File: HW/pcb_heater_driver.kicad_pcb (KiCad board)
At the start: 2 copper layers, 160 x 100 mm, 64 parts, among them J1 Heater, J2 JTAG, J4 USB_C_Receptacle_USB2.0, J5 OLED, Q1 RQ3E110AJ, Q2 BC817, Q3 BC817, SW1 SW_SPST, SW2 SW_DPST, SW3 SW_DPST, SW4 SW_SPST, SW5 SW_SPST, U1 ESP32-S2-MINI-2, U2 TS30042-M000QFNR, U3 CH340C, U4 fork_p5.0mm, U5 fork_p5.0mm

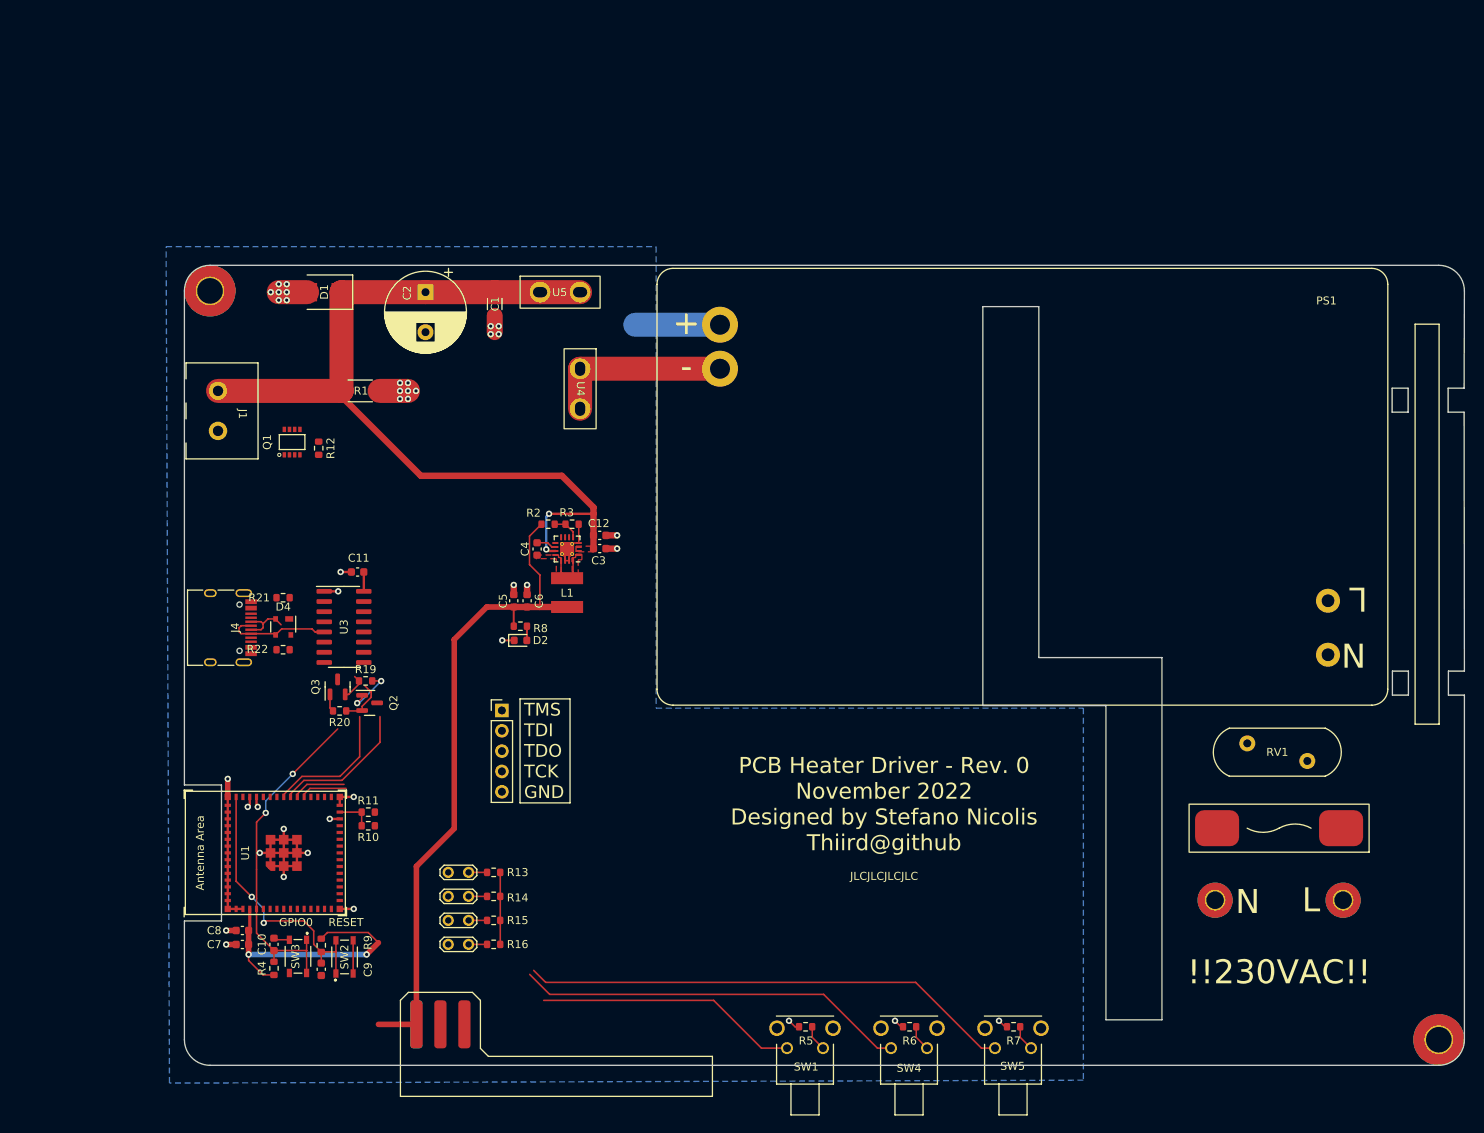
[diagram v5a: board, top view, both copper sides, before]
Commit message: Finished routing, only mosfet left, fixed layout, outline
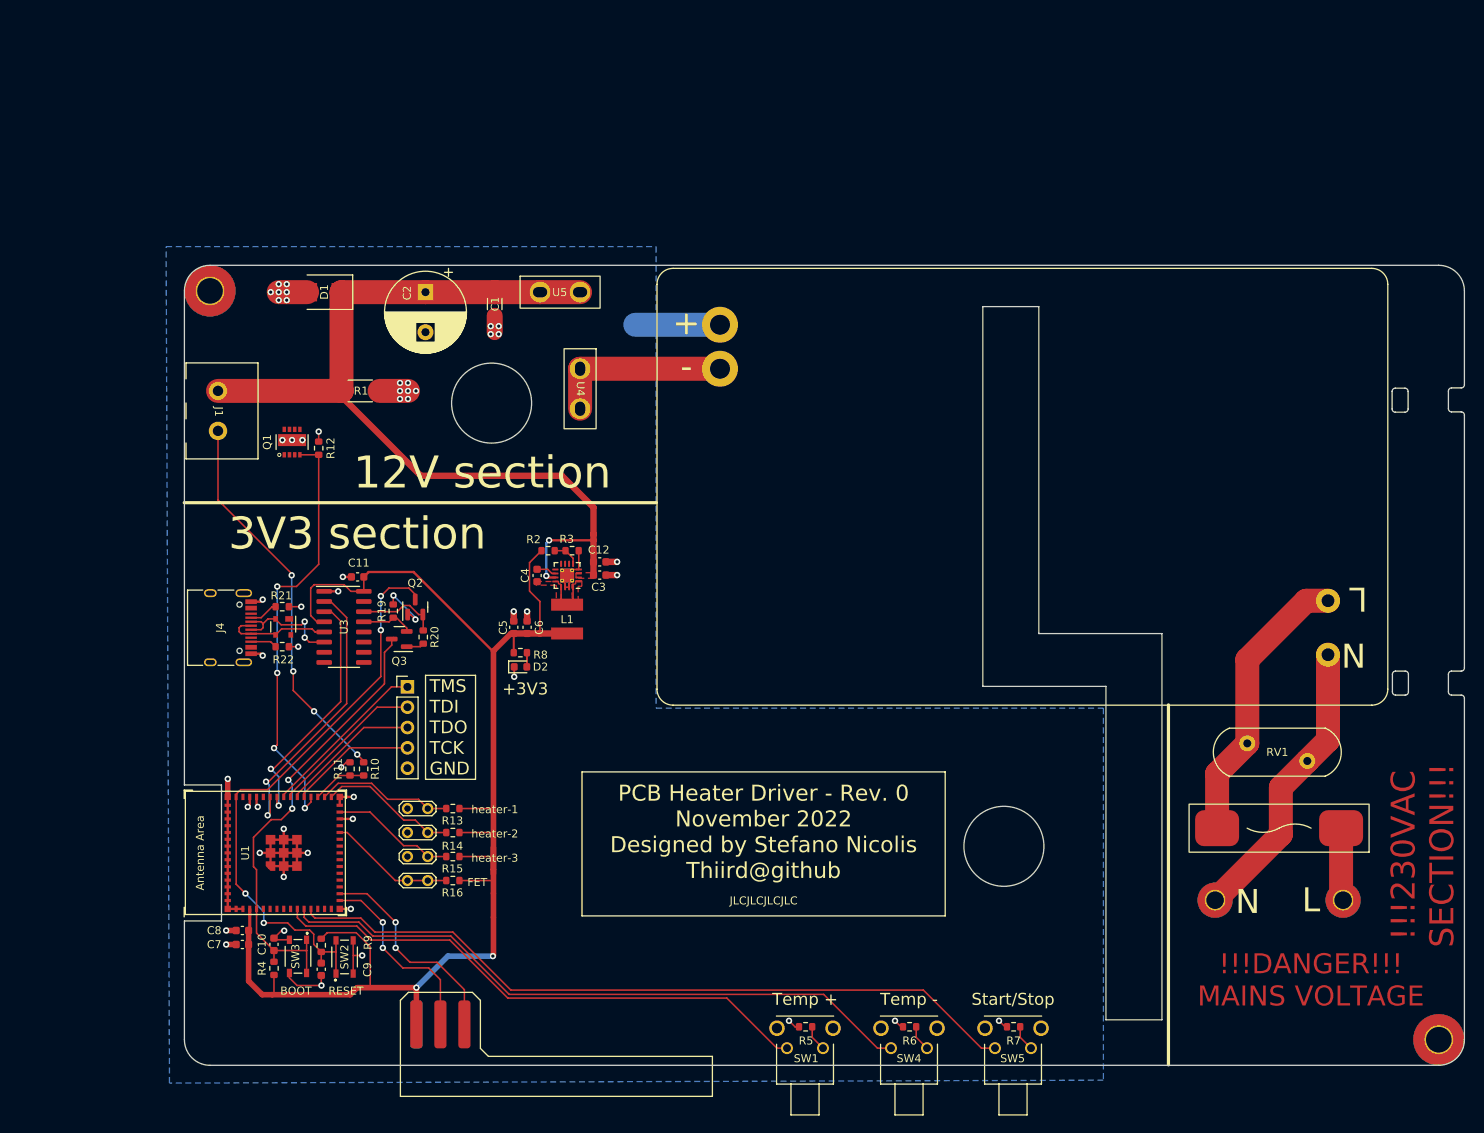
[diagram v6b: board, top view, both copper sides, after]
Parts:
- moved R20 13.9 mm to (103.0, 91.6), turned to -90 degrees
- moved Q2 13.3 mm to (102.0, 87.9), turned to 90 degrees
- moved J2 12.2 mm to (101.0, 97.8)
- moved Q3 9.75 mm to (100.0, 91.9), turned to 180 degrees
- moved R15 9.47 mm to (106.7, 119.0)
- moved R16 9.47 mm to (106.7, 122.0)
- moved TH1 9.47 mm to (101.0, 113.0)
- moved TH3 9.47 mm to (101.0, 119.0)
- moved TH4 9.47 mm to (101.0, 122.0)
- moved R13 9.47 mm to (106.7, 113.0)
- moved R14 9.47 mm to (106.7, 116.0)
- moved TH2 9.47 mm to (101.0, 116.0)
- moved R19 9.39 mm to (99.2, 88.4), turned to 90 degrees
- moved R10 7.13 mm to (95.5, 108.1), turned to -90 degrees
- moved R11 5.86 mm to (93.8, 108.1), turned to 90 degrees
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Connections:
- SW5 pad 1: user_action -> start_stop
- U1 pad 10: user_action -> temperature_plus
- U1 pad 11: temperature_plus -> temperature_minus
- U1 pad 12: temperature_minus -> start_stop
- U1 pad 29: current_sense_LOW -> temp_heater_3
- U1 pad 31: temp_heater_3 -> temp_heater_2
- U1 pad 32: temp_heater_2 -> temp_heater_1
- U1 pad 33: temp_heater_1 -> current_sense_LOW
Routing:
- net start_stop: track 0.00 -> 93.1 mm
- net user_action: track 61.7 -> 0.00 mm
- net GPIO0: track 0.29 -> 58.2 mm, vias 0 -> 2
- net mosfet_gate: track 0.00 -> 53.5 mm, vias 0 -> 4
- net /Heater/heater_LOW: track 0.00 -> 49.0 mm, vias 0 -> 7
- net +3V3: track 131.3 -> 179.4 mm
- net RESET: track 34.7 -> 74.5 mm, vias 2 -> 4
- net Net-(H7-Pad1): track 0.00 -> 36.5 mm
- net temperature_plus: track 32.9 -> 69.1 mm
- net Net-(F1-Pad2): track 0.00 -> 35.8 mm
- net RX: track 0.00 -> 35.4 mm, vias 0 -> 2
- net temperature_minus: track 49.0 -> 81.2 mm
- net TX: track 0.00 -> 31.0 mm, vias 0 -> 2
- net SDA: track 0.00 -> 26.8 mm, vias 0 -> 2
- net GND: track 142.4 -> 116.9 mm, vias 42 -> 49
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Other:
- outline, holes or cut-outs redrawn
- board text added: "!!!230VAC SECTION!!!"
- board text added: "!!!DANGER!!! MAINS VOLTAGE"
- board text added: "+3V3"
- board text added: "12V section"
- board text added: "3V3 section"
- board text added: "BOOT"
- board text added: "FET"
- board text added: "Start/Stop"
- board text added: "Temp +"
- board text added: "Temp -"
- board text added: "heater-1"
- board text added: "heater-2"
- board text added: "heater-3"
- board text removed: "!!230VAC!!"
- board text removed: "GPIO0"

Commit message: Fix board, QOL fixes
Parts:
- moved R10 6.69 mm to (88.9, 109.2), turned to 180 degrees
- moved SW2 5.65 mm to (87.5, 131.5), turned to -90 degrees
- moved R11 4.94 mm to (88.9, 107.5), turned to 0 degrees
- moved SW3 4.73 mm to (82.6, 131.5)
- moved U1 4.73 mm to (80.8, 118.6)
- moved C10 4.73 mm to (79.6, 130.0)
- moved C7 4.73 mm to (75.6, 130.0)
- moved C8 4.73 mm to (75.6, 128.3)
- moved R4 4.73 mm to (79.6, 133.0)
- moved C9 3.17 mm to (90.4, 130.0), turned to 90 degrees
- moved R9 2.84 mm to (90.4, 133.0), turned to 90 degrees
- moved Q1 0.83 mm to (87.1, 66.6)
- moved R12 0.83 mm to (90.5, 67.4)
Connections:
- U1 pad 28: GND -> unconnected-(U1-Pad28)
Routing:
- net +3V3: track 179.4 -> 172.3 mm
- net RESET: track 74.5 -> 81.0 mm
- net /MCU/TMS: track 21.3 -> 26.4 mm
- net /MCU/TCK: track 15.7 -> 20.6 mm
- net /MCU/TDO: track 17.6 -> 22.4 mm
- net /MCU/TDI: track 19.5 -> 24.3 mm
- net temp_heater_3: track 15.6 -> 20.3 mm
- net start_stop: track 93.1 -> 97.8 mm
- net temp_mosfet: track 15.8 -> 20.5 mm
- net temperature_plus: track 69.1 -> 73.7 mm
- net temp_heater_1: track 17.2 -> 21.9 mm
- net temperature_minus: track 81.2 -> 85.7 mm
- net SCL: track 24.1 -> 28.6 mm
- net temp_heater_2: track 17.3 -> 21.8 mm
- net GPIO0: track 58.2 -> 62.4 mm
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- added copper zone on B.Cu, net /Heater/heater_LOW
- added copper zone on F.Cu, net /Heater/heater_LOW
- added copper zone on F.Cu, net GND
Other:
- outline, holes or cut-outs redrawn

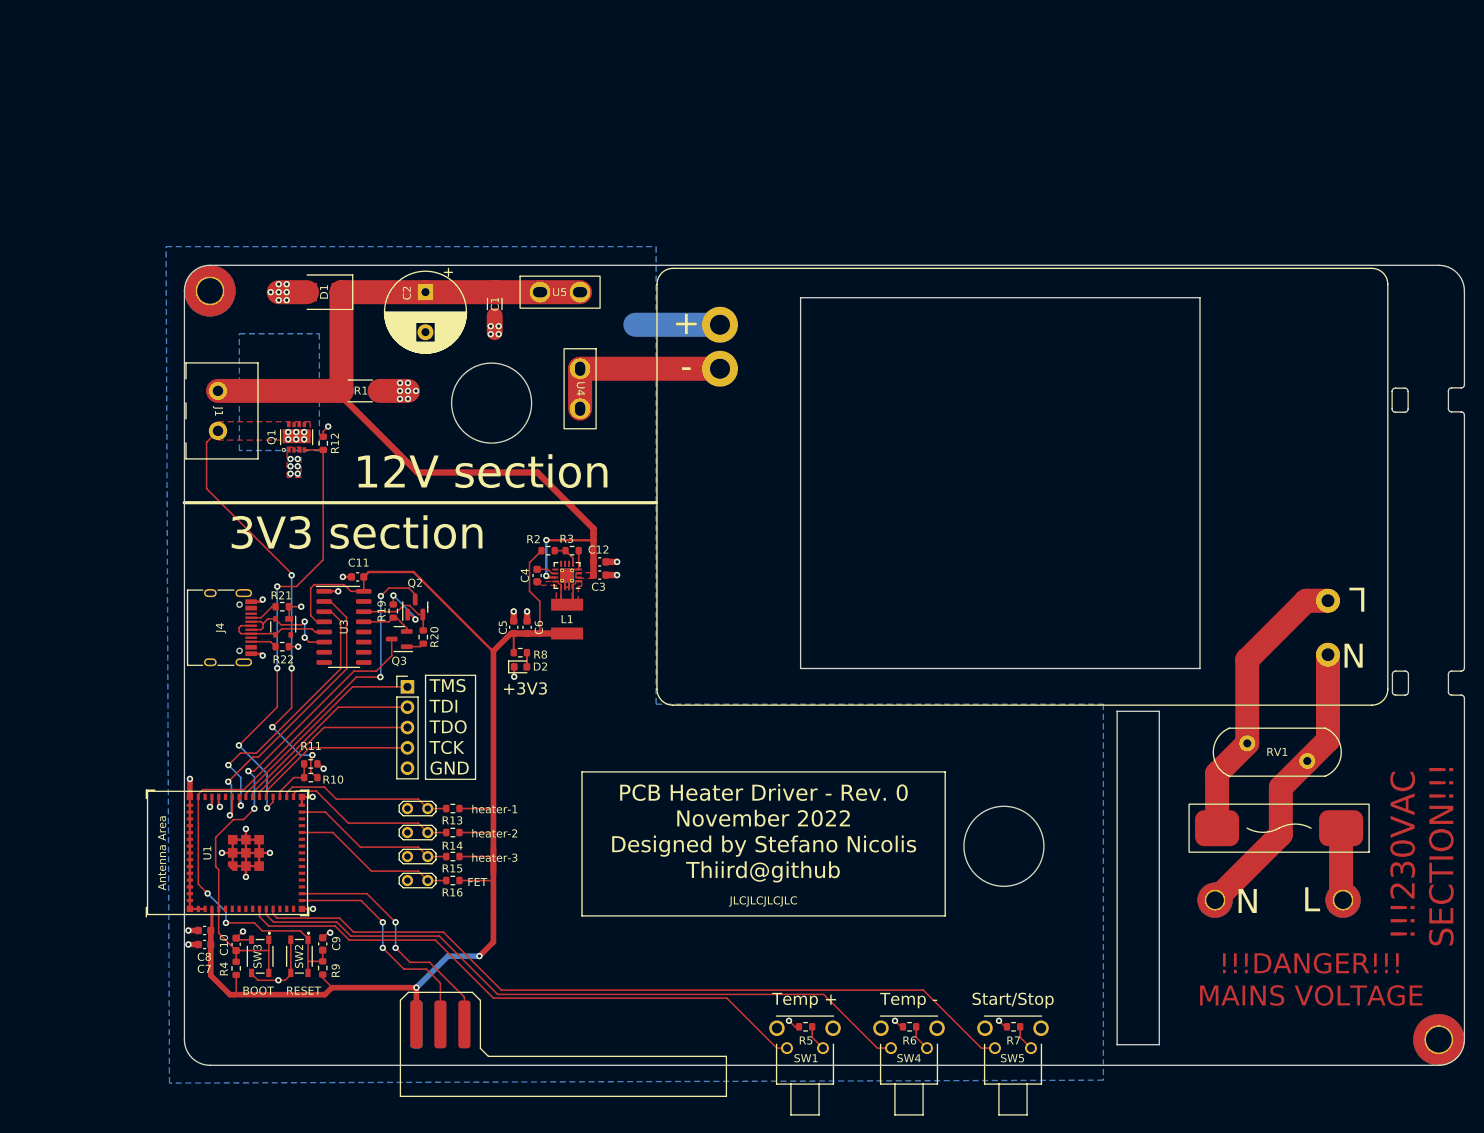
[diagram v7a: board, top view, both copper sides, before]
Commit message: QOL changes on pcb, fixed wrong ACDC brick polarity xD
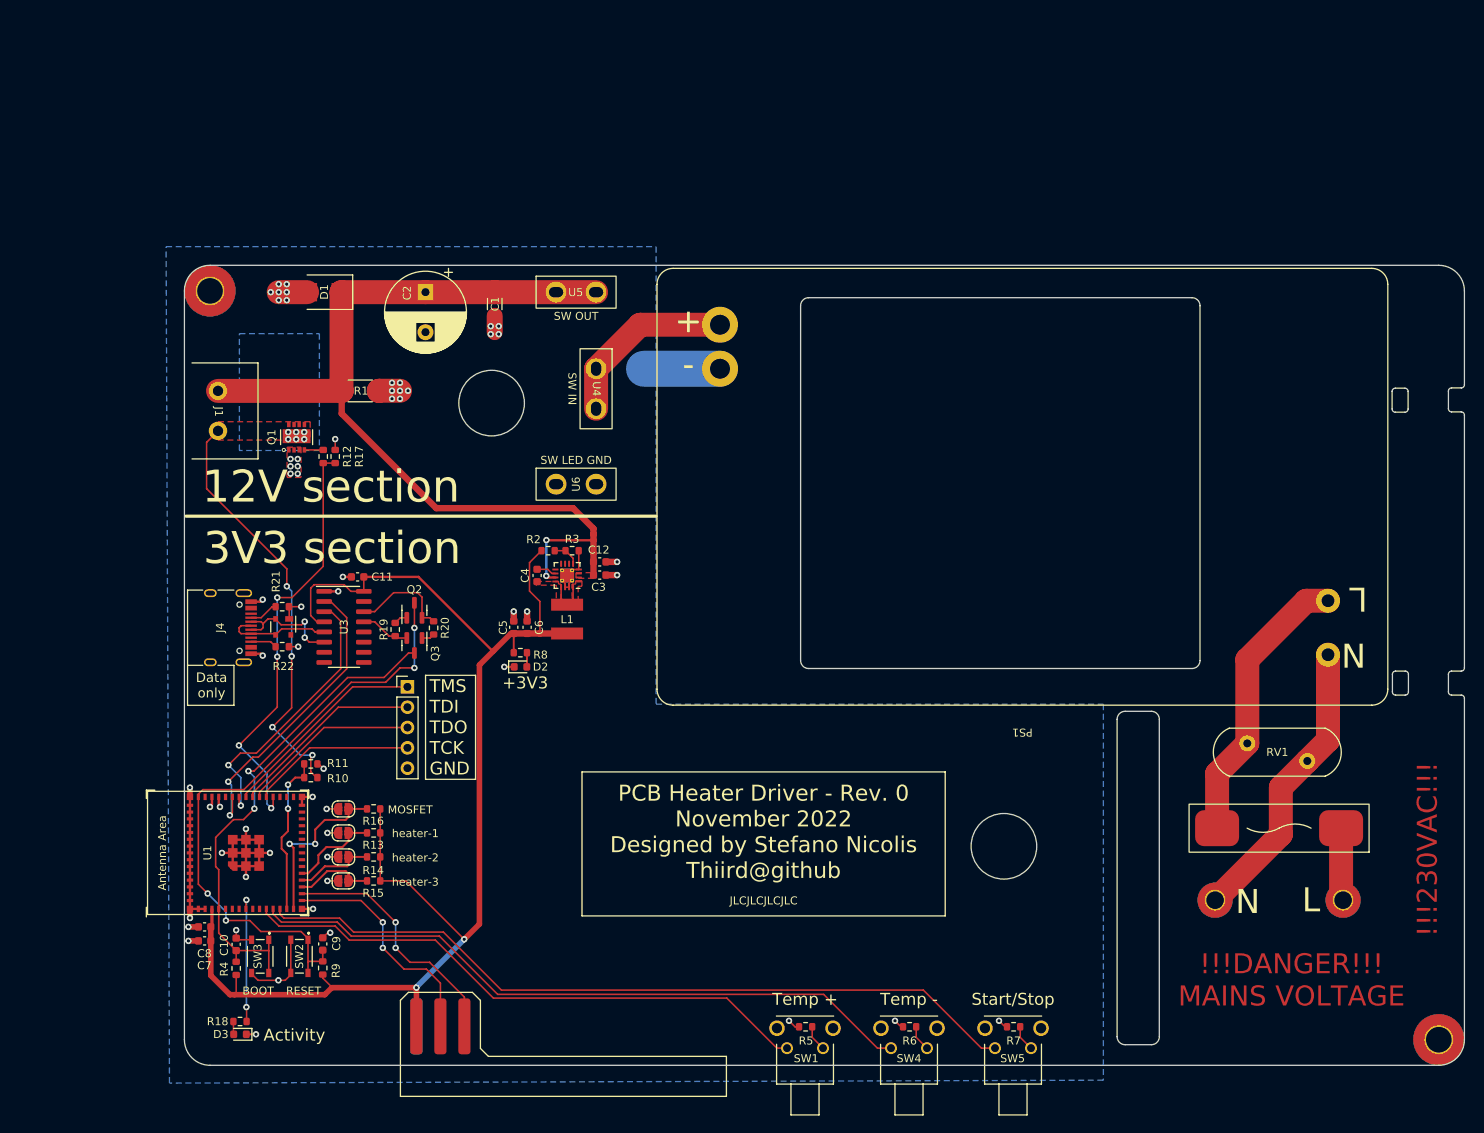
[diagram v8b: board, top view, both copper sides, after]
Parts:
- added D3: RED, LED_SMD:LED_0603_1608Metric, F.Cu at (80.1, 141.3)
- added R17: TBD, Resistor_SMD:R_0603_1608Metric, F.Cu at (90.5, 69.0)
- added R18: 1k, Resistor_SMD:R_0603_1608Metric, F.Cu at (80.1, 139.7)
- added U6: fork_p5.0mm, fork_connector_p5.0mm:fork_p5.0mm, F.Cu at (122.1, 72.5)
- R10: value 100k -> 22k
- R11: value 37k -> 5k1
- TH1, TH2, TH3, TH4: footprint TestPoint:TestPoint_2Pads_Pitch2.54mm_Drill0.8mm -> Jumper:SolderJumper-2_P1.3mm_Open_RoundedPad1.0x1.5mm
- moved R16 13.4 mm to (96.8, 113.1)
- moved TH4 12.0 mm to (93.0, 113.1)
- moved R15 10.4 mm to (96.8, 122.1)
- moved R13 10.4 mm to (96.8, 116.1)
- moved R14 10.4 mm to (96.8, 119.1)
- moved TH1 8.56 mm to (93.0, 116.1)
- moved TH3 8.56 mm to (93.0, 122.1)
- moved TH2 8.56 mm to (93.0, 119.1)
- moved R19 2.32 mm to (99.5, 90.7)
- moved R12 2.23 mm to (92.0, 69.0)
- moved Q3 2.06 mm to (101.9, 92.7), turned to -90 degrees
- moved U4 2.00 mm to (124.6, 60.6)
- moved U5 2.00 mm to (122.1, 48.5)
- moved R20 1.73 mm to (104.3, 90.5)
- moved C7 0.45 mm to (75.6, 129.6)
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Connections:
- PS1 pad 3: GND -> Net-(PS1-Pad3)
- PS1 pad 4: Net-(PS1-Pad4) -> GND
- Q1 pad 2: mosfet_gate -> Net-(Q1-Pad2)
- U1 pad 10: temperature_plus -> unconnected-(U1-Pad10)
- U1 pad 11: temperature_minus -> temperature_plus
- U1 pad 12: start_stop -> temperature_minus
- U1 pad 13: unconnected-(U1-Pad13) -> start_stop
- U1 pad 14: unconnected-(U1-Pad14) -> current_sense_LOW
- U1 pad 15: unconnected-(U1-Pad15) -> temp_mosfet
- U1 pad 18: unconnected-(U1-Pad18) -> temp_heater_3
- U1 pad 19: unconnected-(U1-Pad19) -> temp_heater_2
- U1 pad 20: unconnected-(U1-Pad20) -> temp_heater_1
- U1 pad 23: USB_D- -> unconnected-(U1-Pad23)
- U1 pad 24: USB_D+ -> unconnected-(U1-Pad24)
- U1 pad 26: temp_mosfet -> unconnected-(U1-Pad26)
- U1 pad 29: temp_heater_3 -> unconnected-(U1-Pad29)
- U1 pad 31: temp_heater_2 -> unconnected-(U1-Pad31)
- U1 pad 32: temp_heater_1 -> unconnected-(U1-Pad32)
- U1 pad 33: current_sense_LOW -> unconnected-(U1-Pad33)
- U1 pad 8: unconnected-(U1-Pad8) -> /MCU/activity_led
- U4 pad 1: Net-(PS1-Pad4) -> Net-(PS1-Pad3)
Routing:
- net Net-(PS1-Pad3): track 0.00 -> 22.8 mm
- net Net-(PS1-Pad4): track 22.5 -> 0.00 mm
- net /MCU/activity_led: track 0.00 -> 16.4 mm, vias 0 -> 2
- net current_sense_LOW: track 6.13 -> 20.2 mm, vias 0 -> 2
- net temp_heater_2: track 21.8 -> 9.93 mm
- net temp_heater_1: track 21.9 -> 11.4 mm
- net temp_heater_3: track 20.3 -> 9.96 mm
- net Net-(Q2-Pad1): track 6.50 -> 1.71 mm, vias 2 -> 0
- net GND: track 115.5 -> 119.9 mm, vias 54 -> 60
- net +12V: track 114.2 -> 117.4 mm
- net RESET: track 81.0 -> 77.9 mm
- net mosfet_gate: track 56.1 -> 53.2 mm
- net /Peripherals/RTS: track 10.2 -> 12.7 mm
- net Net-(Q1-Pad2): track 0.00 -> 2.35 mm
- net Net-(D3-Pad2): track 0.00 -> 1.62 mm
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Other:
- outline, holes or cut-outs redrawn
- board text added: "!!!230VAC!!!"
- board text added: "Activity"
- board text added: "Data only"
- board text added: "MOSFET"
- board text added: "SW IN"
- board text added: "SW LED GND"
- board text added: "SW OUT"
- board text removed: "!!!230VAC SECTION!!!"
- board text removed: "FET"
